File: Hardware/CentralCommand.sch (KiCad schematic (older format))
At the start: 18 parts, among them P101 CONN_01X10, P102 CONN_01X10, P103 CONN_01X04, P104 CONN_01X02, P105 CONN_01X04, P106 CONN_01X02, U101 STM32F030C8, Y101 Crystal

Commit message: Rename project files to remove the space between 'Central' & 'Command' for the XSL processing of the BOM
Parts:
- C101: value C -> .1U
- L101: value INDUCTOR -> 10uH
- U101: MPN (none) -> STM32F030C8
- U101: Link (none) -> https://parts.io/detail/153811934/STM32F030C8T6TR; MPN (none) -> STM32F030C8
- Y101: MPN (none) -> FOXSLF/080-20
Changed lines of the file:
@@
 EESchema Schematic File Version 2
-LIBS:Central Command-rescue
 LIBS:power
 LIBS:device
@@
 LIBS:valves
 LIBS:stm32f030c8
-LIBS:Central Command-cache
+LIBS:CentralCommand-cache
 EELAYER 25 0
 EELAYER END
@@
 P 4400 700
 F 0 "L101" V 4350 700 50  0000 C CNN
-F 1 "INDUCTOR" V 4500 700 50  0000 C CNN
+F 1 "10uH" V 4500 700 50  0000 C CNN
 F 2 "Inductors_NEOSID:Neosid_Inductor_SM1206" H 4400 700 60  0001 C CNN
 F 3 "" H 4400 700 60  0000 C CNN
@@
 P 5150 850
 F 0 "C101" H 5175 950 50  0000 L CNN
-F 1 "C" H 5175 750 50  0000 L CNN
+F 1 ".1U" H 5175 750 50  0000 L CNN
 F 2 "Capacitors_SMD:C_0805" H 5188 700 30  0001 C CNN
 F 3 "" H 5150 850 60  0000 C CNN
@@
 F 2 "Housings_QFP:LQFP-48_7x7mm_Pitch0.5mm" H 4200 4500 60  0001 C CNN
 F 3 "" H 4200 4500 60  0000 C CNN
+F 4 "STM32F030C8" H 4200 4500 60  0001 C CNN "MPN"
 	1    4200 4500
 	1    0    0    -1
@@
 F 2 "Housings_QFP:LQFP-48_7x7mm_Pitch0.5mm" H 4200 1950 60  0001 C CNN
 F 3 "" H 4200 1950 60  0000 C CNN
+F 4 "STM32F030C8" H 4200 1950 60  0001 C CNN "MPN"
+F 5 "https://parts.io/detail/153811934/STM32F030C8T6TR" H 4200 1950 60  0001 C CNN "Link"
 	3    4200 1950
 	1    0    0    -1
@@
 F 2 "Crystals:Crystal_HC49-U_Vertical" H 5800 1650 60  0001 C CNN
 F 3 "" H 5800 1650 60  0000 C CNN
-F 4 "http://parts.io/detail/343558/FOXSLF%2F080-20" H 5800 1650 60  0001 C CNN "Link"
+F 4 "FOXSLF/080-20" H 5800 1650 60  0001 C CNN "MPN"
+F 5 "http://parts.io/detail/343558/FOXSLF%2F080-20" H 5800 1650 60  0001 C CNN "Link"
 	1    5800 1650
 	0    1    1    0

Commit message: - Added Farnell and digi-key supplier numbers to most past. Still need todo crystal, switch and micro inductor. - updated the HTML BOM and CSV
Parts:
- C101, C104, C107: Farnell (none) -> 2496944; MPN (none) -> 0805B104K500CT
- C102, C103: Farnell (none) -> 2332762; MPN (none) -> 08055A200JAT2A
- C105, C108: Farnell (none) -> 1856632; MPN (none) -> MCSH31B105K100CT
- C106, C109: Farnell (none) -> 2320921; MPN (none) -> MC1206B106K160CT
- P101, P102: Farnell (none) -> 1022261; MPN (none) -> M20-9991046
- P103, P105: Farnell (none) -> 1022251; MPN (none) -> M20-9990446
- P104, P106: Farnell (none) -> 1022247; MPN (none) -> M20-9990246
- U101: Farnell (none) -> 2393634
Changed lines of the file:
@@
 F 2 "Capacitors_SMD:C_0805" H 5188 700 30  0001 C CNN
 F 3 "" H 5150 850 60  0000 C CNN
+F 4 "2496944" H 5150 850 60  0001 C CNN "Farnell"
+F 5 "0805B104K500CT" H 5150 850 60  0001 C CNN "MPN"
 	1    5150 850
 	1    0    0    -1
@@
 F 3 "" H 4200 4500 60  0000 C CNN
 F 4 "STM32F030C8" H 4200 4500 60  0001 C CNN "MPN"
+F 5 "2393634" H 4200 4500 60  0001 C CNN "Farnell"
 	1    4200 4500
 	1    0    0    -1
@@
 F 2 "Capacitors_SMD:C_0805" H 6288 1300 30  0001 C CNN
 F 3 "" H 6250 1450 60  0000 C CNN
+F 4 "2332762" H 6250 1450 60  0001 C CNN "Farnell"
+F 5 "08055A200JAT2A" H 6250 1450 60  0001 C CNN "MPN"
 	1    6250 1450
 	0    1    1    0
@@
 F 2 "Capacitors_SMD:C_0805" H 6288 1750 30  0001 C CNN
 F 3 "" H 6250 1900 60  0000 C CNN
+F 4 "2332762" H 6250 1900 60  0001 C CNN "Farnell"
+F 5 "08055A200JAT2A" H 6250 1900 60  0001 C CNN "MPN"
 	1    6250 1900
 	0    1    1    0
@@
 F 2 "Pin_Headers:Pin_Header_Straight_1x10" H 1300 1850 60  0001 C CNN
 F 3 "" H 1300 1850 60  0000 C CNN
+F 4 "1022261" H 1300 1850 60  0001 C CNN "Farnell"
+F 5 "M20-9991046" H 1300 1850 60  0001 C CNN "MPN"
 	1    1300 1850
 	-1   0    0    -1
@@
 F 2 "Pin_Headers:Pin_Header_Straight_1x04" H 5850 3900 60  0001 C CNN
 F 3 "" H 5850 3900 60  0000 C CNN
+F 4 "1022251" H 5850 3900 60  0001 C CNN "Farnell"
+F 5 "M20-9990446" H 5850 3900 60  0001 C CNN "MPN"
 	1    5850 3900
 	-1   0    0    -1
@@
 F 2 "Pin_Headers:Pin_Header_Straight_1x04" H 5800 5200 60  0001 C CNN
 F 3 "" H 5800 5200 60  0000 C CNN
+F 4 "1022251" H 5800 5200 60  0001 C CNN "Farnell"
+F 5 "M20-9990446" H 5800 5200 60  0001 C CNN "MPN"
 	1    5800 5200
 	-1   0    0    -1
@@
 F 2 "Pin_Headers:Pin_Header_Straight_1x02" H 7150 5300 60  0001 C CNN
 F 3 "" H 7150 5300 60  0000 C CNN
+F 4 "1022247" H 7150 5300 60  0001 C CNN "Farnell"
+F 5 "M20-9990246" H 7150 5300 60  0001 C CNN "MPN"
 	1    7150 5300
 	-1   0    0    -1
@@
 F 2 "Pin_Headers:Pin_Header_Straight_1x10" H 950 5400 60  0001 C CNN
 F 3 "" H 950 5400 60  0000 C CNN
+F 4 "1022261" H 950 5400 60  0001 C CNN "Farnell"
+F 5 "M20-9991046" H 950 5400 60  0001 C CNN "MPN"
 	1    950  5400
 	-1   0    0    -1
@@
 F 2 "Pin_Headers:Pin_Header_Straight_1x02" H 5800 7250 60  0001 C CNN
 F 3 "" H 5800 7250 60  0000 C CNN
+F 4 "1022247" H 5800 7250 60  0001 C CNN "Farnell"
+F 5 "M20-9990246" H 5800 7250 60  0001 C CNN "MPN"
 	1    5800 7250
 	-1   0    0    -1
@@
 F 2 "Capacitors_SMD:C_0805" H 8138 850 30  0001 C CNN
 F 3 "" H 8100 1000 60  0000 C CNN
+F 4 "2496944" H 8100 1000 60  0001 C CNN "Farnell"
+F 5 "0805B104K500CT" H 8100 1000 60  0001 C CNN "MPN"
 	1    8100 1000
 	1    0    0    -1
@@
 F 2 "Capacitors_SMD:C_1206" H 8438 850 30  0001 C CNN
 F 3 "" H 8400 1000 60  0000 C CNN
+F 4 "1856632" H 8400 1000 60  0001 C CNN "Farnell"
+F 5 "MCSH31B105K100CT" H 8400 1000 60  0001 C CNN "MPN"
 	1    8400 1000
 	1    0    0    -1
@@
 F 2 "Capacitors_SMD:C_1206" H 8738 850 30  0001 C CNN
 F 3 "" H 8700 1000 60  0000 C CNN
+F 4 "2320921" H 8700 1000 60  0001 C CNN "Farnell"
+F 5 "MC1206B106K160CT" H 8700 1000 60  0001 C CNN "MPN"
 	1    8700 1000
 	1    0    0    -1
@@
 F 2 "Capacitors_SMD:C_0805" H 9488 850 30  0001 C CNN
 F 3 "" H 9450 1000 60  0000 C CNN
+F 4 "2496944" H 9450 1000 60  0001 C CNN "Farnell"
+F 5 "0805B104K500CT" H 9450 1000 60  0001 C CNN "MPN"
 	1    9450 1000
 	1    0    0    -1
@@
 F 2 "Capacitors_SMD:C_1206" H 9738 850 30  0001 C CNN
 F 3 "" H 9700 1000 60  0000 C CNN
+F 4 "1856632" H 9700 1000 60  0001 C CNN "Farnell"
+F 5 "MCSH31B105K100CT" H 9700 1000 60  0001 C CNN "MPN"
 	1    9700 1000
 	1    0    0    -1
@@
 F 2 "Capacitors_SMD:C_1206" H 9988 850 30  0001 C CNN
 F 3 "" H 9950 1000 60  0000 C CNN
+F 4 "2320921" H 9950 1000 60  0001 C CNN "Farnell"
+F 5 "MC1206B106K160CT" H 9950 1000 60  0001 C CNN "MPN"
 	1    9950 1000
 	1    0    0    -1

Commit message: Added the farnell code for the last few parts
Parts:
- L101: Farnell (none) -> 1515399; MPN (none) -> LQH31CN100K03L
- Y101: Farnell (none) -> 2063945
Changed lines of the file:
@@
 F 2 "Inductors_NEOSID:Neosid_Inductor_SM1206" H 4400 700 60  0001 C CNN
 F 3 "" H 4400 700 60  0000 C CNN
+F 4 "1515399" V 4400 700 60  0001 C CNN "Farnell"
+F 5 "LQH31CN100K03L" V 4400 700 60  0001 C CNN "MPN"
 	1    4400 700
 	0    -1   -1   0
@@
 F 4 "FOXSLF/080-20" H 5800 1650 60  0001 C CNN "MPN"
 F 5 "http://parts.io/detail/343558/FOXSLF%2F080-20" H 5800 1650 60  0001 C CNN "Link"
+F 6 "2063945" H 5800 1650 60  0001 C CNN "Farnell"
 	1    5800 1650
 	0    1    1    0

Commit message: Tested changing value to the MPN
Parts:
- C102, C103: value 20P -> 08055A200JAT2A
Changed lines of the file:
@@
 P 6250 1450
 F 0 "C102" H 6275 1550 50  0000 L CNN
-F 1 "20P" H 6275 1350 50  0000 L CNN
+F 1 "08055A200JAT2A" H 6275 1350 50  0000 L CNN
 F 2 "Capacitors_SMD:C_0805" H 6288 1300 30  0001 C CNN
 F 3 "" H 6250 1450 60  0000 C CNN
-F 4 "2332762" H 6250 1450 60  0001 C CNN "Farnell"
-F 5 "08055A200JAT2A" H 6250 1450 60  0001 C CNN "MPN"
+F 4 "08055A200JAT2A" H 6250 1450 60  0001 C CNN "MPN"
+F 5 "2332762" H 6250 1450 60  0001 C CNN "Farnell"
 	1    6250 1450
 	0    1    1    0
@@
 P 6250 1900
 F 0 "C103" H 6275 2000 50  0000 L CNN
-F 1 "20P" H 6275 1800 50  0000 L CNN
+F 1 "08055A200JAT2A" H 6275 1800 50  0000 L CNN
 F 2 "Capacitors_SMD:C_0805" H 6288 1750 30  0001 C CNN
 F 3 "" H 6250 1900 60  0000 C CNN
-F 4 "2332762" H 6250 1900 60  0001 C CNN "Farnell"
-F 5 "08055A200JAT2A" H 6250 1900 60  0001 C CNN "MPN"
+F 4 "08055A200JAT2A" H 6250 1900 60  0001 C CNN "MPN"
+F 5 "2332762" H 6250 1900 60  0001 C CNN "Farnell"
 	1    6250 1900
 	0    1    1    0

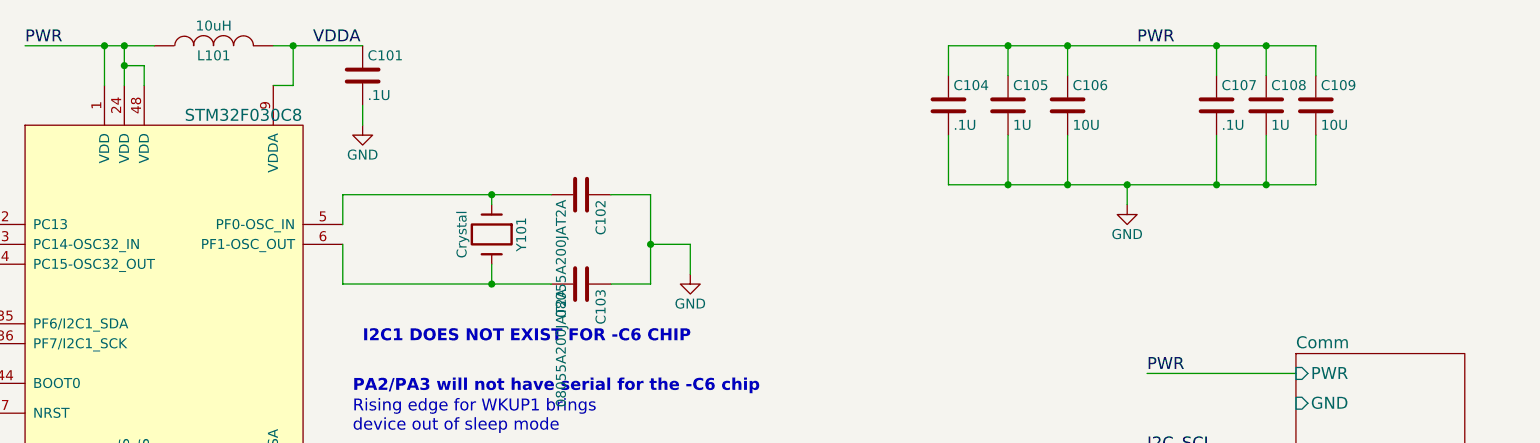
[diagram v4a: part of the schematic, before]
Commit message: Changed the component values to hold MPNs for Macrofab processing
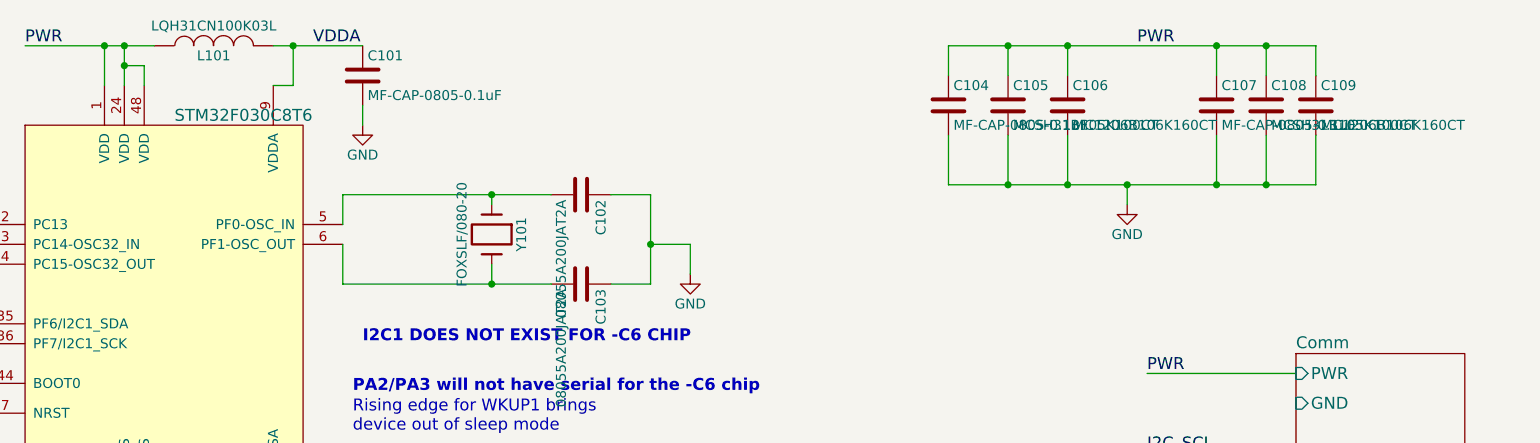
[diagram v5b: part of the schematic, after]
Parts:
- C101, C104, C107: value .1U -> MF-CAP-0805-0.1uF
- C105, C108: value 1U -> MCSH31B105K100CT
- C106, C109: value 10U -> MC1206B106K160CT
- L101: value 10uH -> LQH31CN100K03L
- U101: value STM32F030C8 -> STM32F030C8T6
- Y101: value Crystal -> FOXSLF/080-20
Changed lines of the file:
@@
 P 4400 700
 F 0 "L101" V 4350 700 50  0000 C CNN
-F 1 "10uH" V 4500 700 50  0000 C CNN
+F 1 "LQH31CN100K03L" V 4500 700 50  0000 C CNN
 F 2 "Inductors_NEOSID:Neosid_Inductor_SM1206" H 4400 700 60  0001 C CNN
 F 3 "" H 4400 700 60  0000 C CNN
-F 4 "1515399" V 4400 700 60  0001 C CNN "Farnell"
-F 5 "LQH31CN100K03L" V 4400 700 60  0001 C CNN "MPN"
+F 4 "LQH31CN100K03L" V 4400 700 60  0001 C CNN "MPN"
+F 5 "1515399" V 4400 700 60  0001 C CNN "Farnell"
 	1    4400 700
 	0    -1   -1   0
@@
 P 5150 850
 F 0 "C101" H 5175 950 50  0000 L CNN
-F 1 ".1U" H 5175 750 50  0000 L CNN
+F 1 "MF-CAP-0805-0.1uF" H 5175 750 50  0000 L CNN
 F 2 "Capacitors_SMD:C_0805" H 5188 700 30  0001 C CNN
 F 3 "" H 5150 850 60  0000 C CNN
-F 4 "2496944" H 5150 850 60  0001 C CNN "Farnell"
-F 5 "0805B104K500CT" H 5150 850 60  0001 C CNN "MPN"
+F 4 "0805B104K500CT" H 5150 850 60  0001 C CNN "MPN"
+F 5 "2496944" H 5150 850 60  0001 C CNN "Farnell"
 	1    5150 850
 	1    0    0    -1
@@
 P 4200 1950
 F 0 "U101" H 4750 1000 60  0000 C CNN
-F 1 "STM32F030C8" H 4550 2850 60  0000 C CNN
+F 1 "STM32F030C8T6" H 4550 2850 60  0000 C CNN
 F 2 "Housings_QFP:LQFP-48_7x7mm_Pitch0.5mm" H 4200 1950 60  0001 C CNN
 F 3 "" H 4200 1950 60  0000 C CNN
-F 4 "STM32F030C8" H 4200 1950 60  0001 C CNN "MPN"
-F 5 "https://parts.io/detail/153811934/STM32F030C8T6TR" H 4200 1950 60  0001 C CNN "Link"
+F 4 "https://parts.io/detail/153811934/STM32F030C8T6TR" H 4200 1950 60  0001 C CNN "Link"
+F 5 "STM32F030C8" H 4200 1950 60  0001 C CNN "MPN"
 	3    4200 1950
 	1    0    0    -1
@@
 P 5800 1650
 F 0 "Y101" H 5800 1800 50  0000 C CNN
-F 1 "Crystal" H 5800 1500 50  0000 C CNN
+F 1 "FOXSLF/080-20" H 5800 1500 50  0000 C CNN
 F 2 "Crystals:Crystal_HC49-U_Vertical" H 5800 1650 60  0001 C CNN
 F 3 "" H 5800 1650 60  0000 C CNN
-F 4 "FOXSLF/080-20" H 5800 1650 60  0001 C CNN "MPN"
-F 5 "http://parts.io/detail/343558/FOXSLF%2F080-20" H 5800 1650 60  0001 C CNN "Link"
+F 4 "http://parts.io/detail/343558/FOXSLF%2F080-20" H 5800 1650 60  0001 C CNN "Link"
+F 5 "FOXSLF/080-20" H 5800 1650 60  0001 C CNN "MPN"
 F 6 "2063945" H 5800 1650 60  0001 C CNN "Farnell"
 	1    5800 1650
@@
 P 8100 1000
 F 0 "C104" H 8125 1100 50  0000 L CNN
-F 1 ".1U" H 8125 900 50  0000 L CNN
+F 1 "MF-CAP-0805-0.1uF" H 8125 900 50  0000 L CNN
 F 2 "Capacitors_SMD:C_0805" H 8138 850 30  0001 C CNN
 F 3 "" H 8100 1000 60  0000 C CNN
-F 4 "2496944" H 8100 1000 60  0001 C CNN "Farnell"
-F 5 "0805B104K500CT" H 8100 1000 60  0001 C CNN "MPN"
+F 4 "0805B104K500CT" H 8100 1000 60  0001 C CNN "MPN"
+F 5 "2496944" H 8100 1000 60  0001 C CNN "Farnell"
 	1    8100 1000
 	1    0    0    -1
@@
 P 8400 1000
 F 0 "C105" H 8425 1100 50  0000 L CNN
-F 1 "1U" H 8425 900 50  0000 L CNN
+F 1 "MCSH31B105K100CT" H 8425 900 50  0000 L CNN
 F 2 "Capacitors_SMD:C_1206" H 8438 850 30  0001 C CNN
 F 3 "" H 8400 1000 60  0000 C CNN
-F 4 "1856632" H 8400 1000 60  0001 C CNN "Farnell"
-F 5 "MCSH31B105K100CT" H 8400 1000 60  0001 C CNN "MPN"
+F 4 "MCSH31B105K100CT" H 8400 1000 60  0001 C CNN "MPN"
+F 5 "1856632" H 8400 1000 60  0001 C CNN "Farnell"
 	1    8400 1000
 	1    0    0    -1
@@
 P 8700 1000
 F 0 "C106" H 8725 1100 50  0000 L CNN
-F 1 "10U" H 8725 900 50  0000 L CNN
+F 1 "MC1206B106K160CT" H 8725 900 50  0000 L CNN
 F 2 "Capacitors_SMD:C_1206" H 8738 850 30  0001 C CNN
 F 3 "" H 8700 1000 60  0000 C CNN
-F 4 "2320921" H 8700 1000 60  0001 C CNN "Farnell"
-F 5 "MC1206B106K160CT" H 8700 1000 60  0001 C CNN "MPN"
+F 4 "MC1206B106K160CT" H 8700 1000 60  0001 C CNN "MPN"
+F 5 "2320921" H 8700 1000 60  0001 C CNN "Farnell"
 	1    8700 1000
 	1    0    0    -1
@@
 P 9450 1000
 F 0 "C107" H 9475 1100 50  0000 L CNN
-F 1 ".1U" H 9475 900 50  0000 L CNN
+F 1 "MF-CAP-0805-0.1uF" H 9475 900 50  0000 L CNN
 F 2 "Capacitors_SMD:C_0805" H 9488 850 30  0001 C CNN
 F 3 "" H 9450 1000 60  0000 C CNN
-F 4 "2496944" H 9450 1000 60  0001 C CNN "Farnell"
-F 5 "0805B104K500CT" H 9450 1000 60  0001 C CNN "MPN"
+F 4 "0805B104K500CT" H 9450 1000 60  0001 C CNN "MPN"
+F 5 "2496944" H 9450 1000 60  0001 C CNN "Farnell"
 	1    9450 1000
 	1    0    0    -1
@@
 P 9700 1000
 F 0 "C108" H 9725 1100 50  0000 L CNN
-F 1 "1U" H 9725 900 50  0000 L CNN
+F 1 "MCSH31B105K100CT" H 9725 900 50  0000 L CNN
 F 2 "Capacitors_SMD:C_1206" H 9738 850 30  0001 C CNN
 F 3 "" H 9700 1000 60  0000 C CNN
-F 4 "1856632" H 9700 1000 60  0001 C CNN "Farnell"
-F 5 "MCSH31B105K100CT" H 9700 1000 60  0001 C CNN "MPN"
+F 4 "MCSH31B105K100CT" H 9700 1000 60  0001 C CNN "MPN"
+F 5 "1856632" H 9700 1000 60  0001 C CNN "Farnell"
 	1    9700 1000
 	1    0    0    -1
@@
 P 9950 1000
 F 0 "C109" H 9975 1100 50  0000 L CNN
-F 1 "10U" H 9975 900 50  0000 L CNN
+F 1 "MC1206B106K160CT" H 9975 900 50  0000 L CNN
 F 2 "Capacitors_SMD:C_1206" H 9988 850 30  0001 C CNN
 F 3 "" H 9950 1000 60  0000 C CNN
-F 4 "2320921" H 9950 1000 60  0001 C CNN "Farnell"
-F 5 "MC1206B106K160CT" H 9950 1000 60  0001 C CNN "MPN"
+F 4 "MC1206B106K160CT" H 9950 1000 60  0001 C CNN "MPN"
+F 5 "2320921" H 9950 1000 60  0001 C CNN "Farnell"
 	1    9950 1000
 	1    0    0    -1

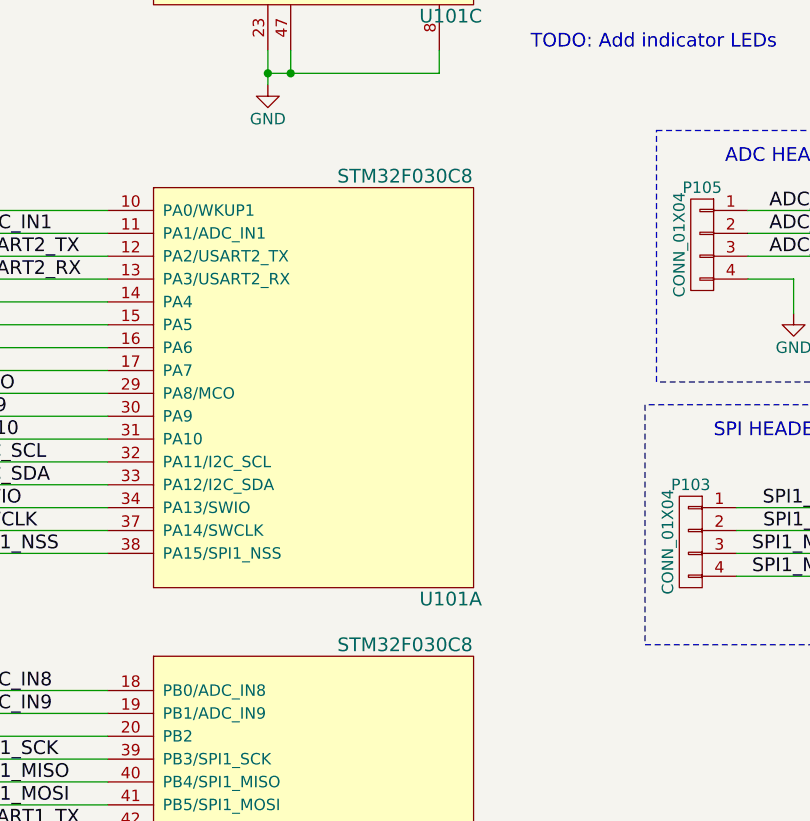
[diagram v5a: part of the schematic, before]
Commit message: Updated layout file, as that's what we're submitting to MF
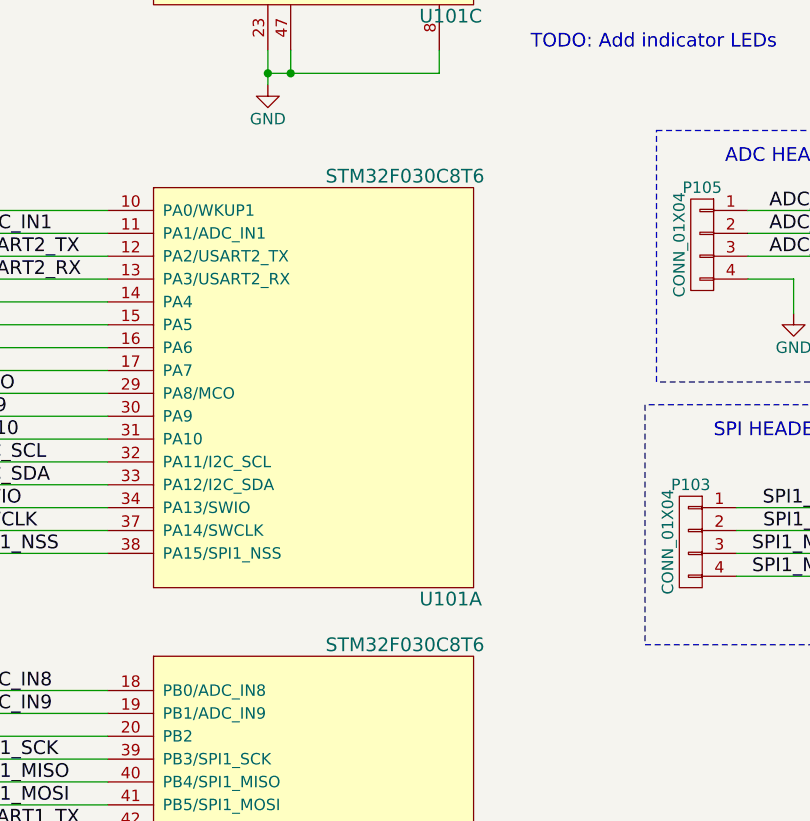
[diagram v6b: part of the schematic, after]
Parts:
- U101: value STM32F030C8 -> STM32F030C8T6
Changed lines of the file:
@@
 $EndComp
 $Comp
-L GND #PWR01
+L GND #PWR1
 U 1 1 5627066D
 P 3950 3200
-F 0 "#PWR01" H 3950 2950 50  0001 C CNN
+F 0 "#PWR1" H 3950 2950 50  0001 C CNN
 F 1 "GND" H 3950 3050 50  0000 C CNN
 F 2 "" H 3950 3200 60  0000 C CNN
@@
 P 4200 4500
 F 0 "U101" H 4750 3550 60  0000 C CNN
-F 1 "STM32F030C8" H 4550 5400 60  0000 C CNN
+F 1 "STM32F030C8T6" H 4550 5400 60  0000 C CNN
 F 2 "Housings_QFP:LQFP-48_7x7mm_Pitch0.5mm" H 4200 4500 60  0001 C CNN
 F 3 "" H 4200 4500 60  0000 C CNN
@@
 P 4200 6550
 F 0 "U101" H 4750 5600 60  0000 C CNN
-F 1 "STM32F030C8" H 4550 7450 60  0000 C CNN
+F 1 "STM32F030C8T6" H 4550 7450 60  0000 C CNN
 F 2 "Housings_QFP:LQFP-48_7x7mm_Pitch0.5mm" H 4200 6550 60  0001 C CNN
 F 3 "" H 4200 6550 60  0000 C CNN
@@
 $EndComp
 $Comp
-L GND #PWR02
+L GND #PWR4
 U 1 1 56529BFD
 P 6800 1850
-F 0 "#PWR02" H 6800 1600 50  0001 C CNN
+F 0 "#PWR4" H 6800 1600 50  0001 C CNN
 F 1 "GND" H 6800 1700 50  0000 C CNN
 F 2 "" H 6800 1850 60  0000 C CNN
@@
 $EndComp
 $Comp
-L GND #PWR03
+L GND #PWR3
 U 1 1 56634940
 P 6250 4200
-F 0 "#PWR03" H 6250 3950 50  0001 C CNN
+F 0 "#PWR3" H 6250 3950 50  0001 C CNN
 F 1 "GND" H 6250 4050 50  0000 C CNN
 F 2 "" H 6250 4200 60  0000 C CNN
@@
 TODO: Add indicator LEDs
 $Comp
-L GND #PWR04
+L GND #PWR2
 U 1 1 56774FCA
 P 5150 1100
-F 0 "#PWR04" H 5150 850 50  0001 C CNN
+F 0 "#PWR2" H 5150 850 50  0001 C CNN
 F 1 "GND" H 5150 950 50  0000 C CNN
 F 2 "" H 5150 1100 60  0000 C CNN
@@
 $EndComp
 $Comp
-L GND #PWR05
+L GND #PWR5
 U 1 1 567FC767
 P 9000 1500
-F 0 "#PWR05" H 9000 1250 50  0001 C CNN
+F 0 "#PWR5" H 9000 1250 50  0001 C CNN
 F 1 "GND" H 9000 1350 50  0000 C CNN
 F 2 "" H 9000 1500 60  0000 C CNN
